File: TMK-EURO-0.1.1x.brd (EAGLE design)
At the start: 100 x 80 mm, 55 parts, among them IC1 TL082P, U1 IN, U2 IN, U3 IN, U4 IN, U5 IN, U6 IN, U7 THONKICONNOLD, X1 057-010-1

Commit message: v0.1.0.1
final V0101
INcluded board., schematic en frontpanel pcb
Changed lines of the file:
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@@
 <layer number="27" name="tValues" color="7" fill="1" visible="yes" active="yes"/>
 <layer number="28" name="bValues" color="7" fill="1" visible="yes" active="yes"/>
-<layer number="29" name="tStop" color="7" fill="3" visible="no" active="yes"/>
-<layer number="30" name="bStop" color="7" fill="6" visible="no" active="yes"/>
+<layer number="29" name="tStop" color="7" fill="3" visible="yes" active="yes"/>
+<layer number="30" name="bStop" color="7" fill="6" visible="yes" active="yes"/>
 <layer number="31" name="tCream" color="7" fill="4" visible="yes" active="yes"/>
 <layer number="32" name="bCream" color="7" fill="5" visible="yes" active="yes"/>
@@
 <text x="44.45" y="3.81" size="1.778" layer="21">1KNOB2MANY</text>
 <text x="12.7" y="1.27" size="1.27" layer="21" ratio="7">sound mangling ultra drive feedback gain  resonator</text>
+<text x="17.78" y="45.72" size="1.778" layer="25">+</text>
 </plain>
 <attributes>
@@
 </element>
 <element name="C1" library="adafruit" package="E2-5" value="10uF" x="15.24" y="44.45" smashed="yes" rot="R270">
-<attribute name="NAME" x="10.16" y="42.926" size="1.27" layer="25" ratio="10"/>
+<attribute name="NAME" x="11.43" y="41.656" size="1.27" layer="25" ratio="10"/>
 </element>
 <element name="C9" library="rcl" package="C050-035X075" value="100nF" x="91.44" y="59.69" smashed="yes" rot="R180">
@@
 <vertex x="1.27" y="77.47"/>
 <vertex x="1.27" y="0"/>
-<vertex x="99.06" y="1.27"/>
+<vertex x="99.06" y="0.635"/>
 <vertex x="99.06" y="78.74"/>
 <vertex x="24.13" y="78.74"/>
@@
 <contactref element="X1" pad="5"/>
 <contactref element="X1" pad="7"/>
-<via x="20.32" y="64.77" extent="1-16" drill="0.6" shape="square"/>
-<via x="22.86" y="66.04" extent="1-16" drill="0.6" shape="square"/>
-<via x="24.13" y="60.96" extent="1-16" drill="0.6" shape="square"/>
-<via x="26.67" y="63.5" extent="1-16" drill="0.6" shape="square"/>
+<via x="20.32" y="64.77" extent="1-16" drill="0.6" diameter="0.8128" shape="square"/>
+<via x="22.86" y="66.04" extent="1-16" drill="0.6" diameter="0.8128" shape="square"/>
+<via x="24.13" y="60.96" extent="1-16" drill="0.6" diameter="0.8128" shape="square"/>
+<via x="26.67" y="63.5" extent="1-16" drill="0.6" diameter="0.8128" shape="square"/>
 <wire x1="20.32" y1="64.77" x2="21.59" y2="63.5" width="0.6096" layer="1"/>
 <wire x1="21.59" y1="63.5" x2="24.13" y2="60.96" width="0.6096" layer="1"/>
 <wire x1="22.86" y1="66.04" x2="25.4" y2="63.5" width="0.6096" layer="1"/>
 <wire x1="25.4" y1="63.5" x2="26.67" y2="63.5" width="0.6096" layer="1"/>
-<via x="21.59" y="10.16" extent="1-16" drill="0.3048"/>
-<via x="22.86" y="10.16" extent="1-16" drill="0.3048"/>
-<via x="24.13" y="10.16" extent="1-16" drill="0.3048"/>
-<via x="21.59" y="5.08" extent="1-16" drill="0.3048"/>
-<via x="22.86" y="5.08" extent="1-16" drill="0.3048"/>
-<via x="24.13" y="5.08" extent="1-16" drill="0.3048"/>
+<via x="21.59" y="10.16" extent="1-16" drill="0.3048" diameter="0.8128"/>
+<via x="22.86" y="10.16" extent="1-16" drill="0.3048" diameter="0.8128"/>
+<via x="24.13" y="10.16" extent="1-16" drill="0.3048" diameter="0.8128"/>
+<via x="21.59" y="5.08" extent="1-16" drill="0.3048" diameter="0.8128"/>
+<via x="22.86" y="5.08" extent="1-16" drill="0.3048" diameter="0.8128"/>
+<via x="24.13" y="5.08" extent="1-16" drill="0.3048" diameter="0.8128"/>
 <wire x1="21.59" y1="5.08" x2="21.59" y2="6.35" width="0.6096" layer="1"/>
 <wire x1="21.59" y1="6.35" x2="21.59" y2="8.89" width="0.6096" layer="1"/>
@@
 <wire x1="22.86" y1="6.35" x2="22.86" y2="5.08" width="0.6096" layer="1"/>
 <wire x1="24.13" y1="10.16" x2="24.13" y2="8.89" width="0.6096" layer="1"/>
-<via x="21.59" y="8.89" extent="1-16" drill="0.3048"/>
-<via x="22.86" y="8.89" extent="1-16" drill="0.3048"/>
+<via x="21.59" y="8.89" extent="1-16" drill="0.3048" diameter="0.8128"/>
+<via x="22.86" y="8.89" extent="1-16" drill="0.3048" diameter="0.8128"/>
 <wire x1="24.13" y1="8.89" x2="24.13" y2="6.35" width="0.6096" layer="1"/>
-<via x="24.13" y="8.89" extent="1-16" drill="0.3048"/>
-<via x="21.59" y="6.35" extent="1-16" drill="0.3048"/>
-<via x="22.86" y="6.35" extent="1-16" drill="0.3048"/>
+<via x="24.13" y="8.89" extent="1-16" drill="0.3048" diameter="0.8128"/>
+<via x="21.59" y="6.35" extent="1-16" drill="0.3048" diameter="0.8128"/>
+<via x="22.86" y="6.35" extent="1-16" drill="0.3048" diameter="0.8128"/>
 <wire x1="24.13" y1="6.35" x2="24.13" y2="5.08" width="0.6096" layer="1"/>
-<via x="24.13" y="6.35" extent="1-16" drill="0.3048"/>
-<via x="21.59" y="63.5" extent="1-16" drill="0.3048"/>
+<via x="24.13" y="6.35" extent="1-16" drill="0.3048" diameter="0.8128"/>
+<via x="21.59" y="63.5" extent="1-16" drill="0.5" diameter="0.8128"/>
 </signal>
 <signal name="N$2" class="2">

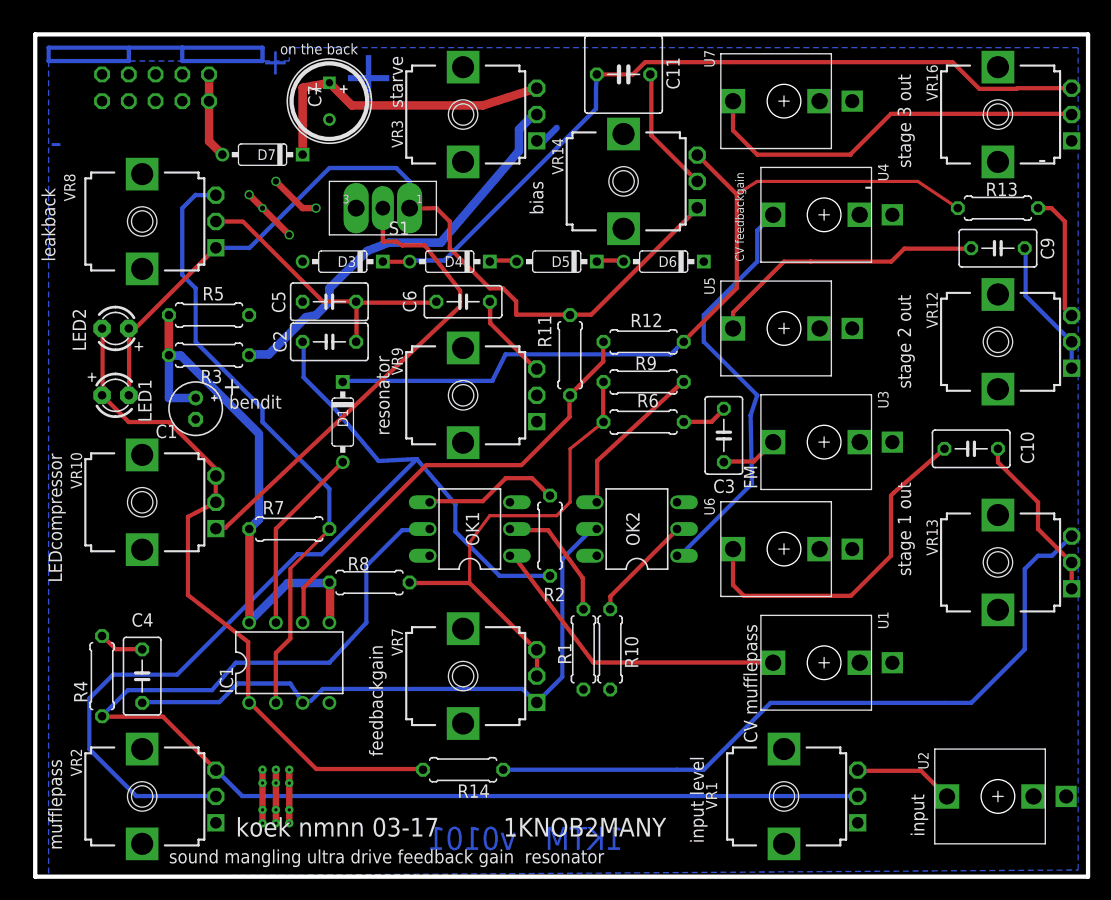
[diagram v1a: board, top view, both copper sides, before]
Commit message: Cleanup for errors
Removed all the CV-inputs. Fixed the power. Check this on breadboard
first!
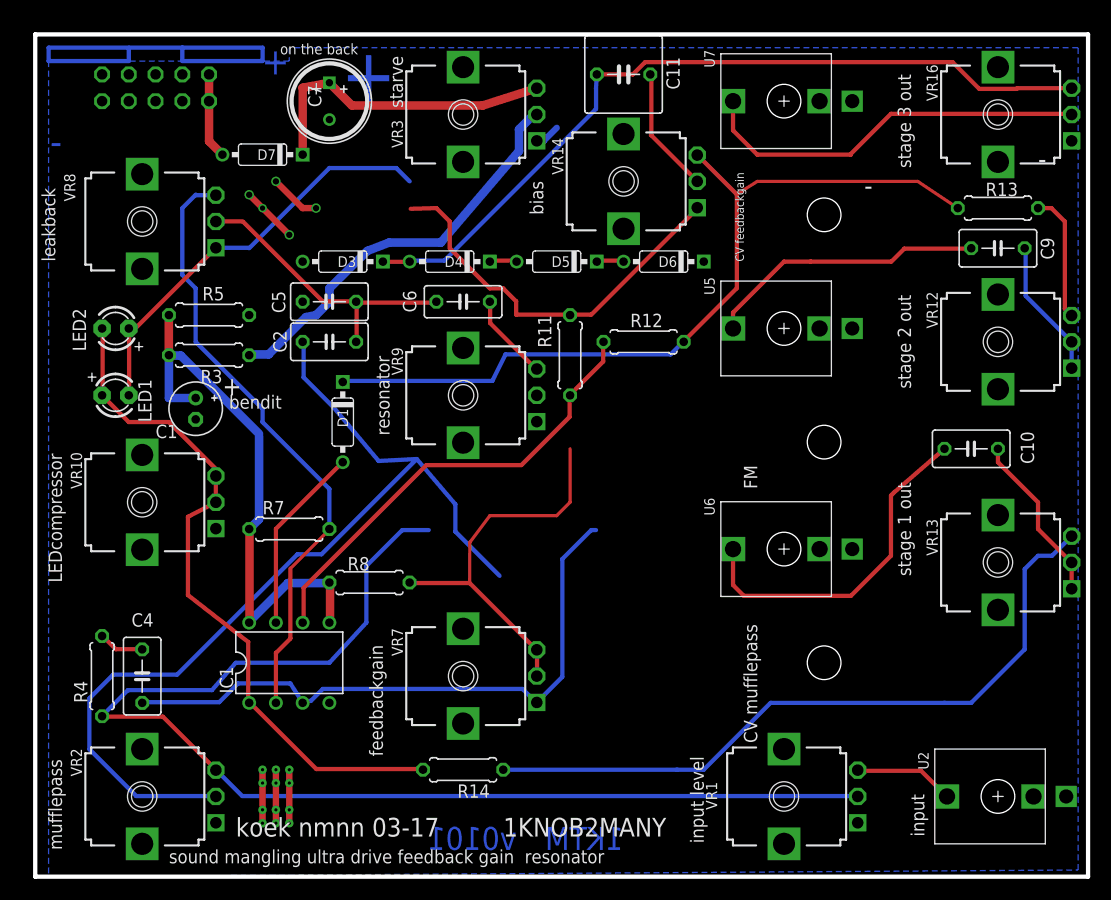
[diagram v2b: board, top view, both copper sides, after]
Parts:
- removed C3: 100nF, rcl:C050-035X075
- removed OK1, OK2: 4N35, optocoupler:DIL06
- removed R1, R10: 5K6, adafruit:0207/7
- removed R2, R9: 3K3, adafruit:0207/7
- removed R6: 10K, adafruit:0207/7
- removed S1: (no value), momentswitchREDlveewrergalmoer mini switch:SPDT
- removed U1, U3, U4: IN, MusicThingModular:THONKICONN
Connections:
- removed net BYPASS: S1.2, VR10.1
- removed net N$27: OK2.4, R9.2
- removed net N$28: OK2.2, R10.1
- removed net N$30: OK2.1, U4.P$3_TIP
- removed net N$31: OK1.4, R2.1
- removed net N$32: OK1.2, R1.1
- removed net N$33: OK1.1, U1.P$3_TIP
- removed net N$34: S1.3
- removed net N$36: C3.1, R6.2
- removed net N$37: C3.2, U3.P$3_TIP
- removed net N$4: C4.2, IC1.3, OK2.5, VR7.1
- new net N$26: C4.2, IC1.3, VR7.1
- net GND: no longer R1.2, R10.2, U1.P$1_SLEEVE, U3.P$1_SLEEVE, U4.P$1_SLEEVE
- net N$2: no longer OK1.5
- net N$5: no longer R6.1, R9.1
- net N$7: now also VR10.1; no longer S1.1
- net N$9: no longer R2.2
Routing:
- net N$4: track 59.5 -> 0.00 mm
- net N$26: track 0.00 -> 59.4 mm
- net BYPASS: track 45.8 -> 0.00 mm
- net N$30: track 40.4 -> 0.00 mm
- net N$33: track 30.1 -> 0.00 mm
- net N$27: track 15.1 -> 0.00 mm
- net N$31: track 13.1 -> 0.00 mm
- net N$32: track 12.3 -> 0.00 mm
- net N$28: track 10.2 -> 0.00 mm
- net N$5: track 45.5 -> 37.5 mm
- net N$37: track 5.47 -> 0.00 mm
- net N$9: track 95.9 -> 91.1 mm
- net N$36: track 4.38 -> 0.00 mm
- net N$7: track 80.6 -> 77.8 mm

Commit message: Fixed power
No Vr on power pin 8, but 12V from the main power supply
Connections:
- net +12V: now also IC1.8
- net VR: no longer IC1.8
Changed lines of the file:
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@@
 <contactref element="R5" pad="1"/>
 <contactref element="C1" pad="+"/>
-<contactref element="IC1" pad="8"/>
 <wire x1="12.6873" y1="53.2638" x2="12.6873" y2="49.6062" width="0.8128" layer="1"/>
 <wire x1="12.6873" y1="49.6062" x2="12.7" y2="49.53" width="0.4064" layer="1"/>
@@
 <wire x1="28.0035" y1="27.8892" x2="27.94" y2="27.94" width="0.4064" layer="1"/>
 <wire x1="20.3454" y1="32.9184" x2="20.3454" y2="24.2316" width="0.8128" layer="1"/>
-<wire x1="20.3454" y1="24.2316" x2="20.32" y2="24.13" width="0.4064" layer="1"/>
 <wire x1="20.3454" y1="32.9184" x2="20.32" y2="33.02" width="0.4064" layer="1"/>
 <wire x1="21.2598" y1="33.9471" x2="21.2598" y2="41.8338" width="0.8128" layer="16"/>
@@
 <wire x1="20.3454" y1="24.2316" x2="24.003" y2="27.8892" width="0.8128" layer="16"/>
 <wire x1="27.8892" y1="27.8892" x2="27.94" y2="27.94" width="0.4064" layer="16"/>
-<wire x1="20.3454" y1="24.2316" x2="20.32" y2="24.13" width="0.4064" layer="16"/>
 <wire x1="13.8303" y1="49.4919" x2="12.8016" y2="49.4919" width="0.8128" layer="16"/>
 <wire x1="21.2598" y1="42.0624" x2="13.8303" y2="49.4919" width="0.8128" layer="16"/>
@@
 <wire x1="12.7" y1="45.466" x2="12.7" y2="49.53" width="0.8128" layer="16"/>
 <wire x1="21.2598" y1="41.8338" x2="21.2598" y2="42.0624" width="0" layer="19" extent="16-16"/>
+<wire x1="20.3454" y1="24.2316" x2="20.3454" y2="24.2316" width="0" layer="19" extent="1-16"/>
 </signal>
 <signal name="N$7" class="1">
@@
 <wire x1="25.4" y1="74.93" x2="27.94" y2="75.41" width="0.8128" layer="1"/>
 <wire x1="25.4" y1="68.58" x2="25.4" y2="74.93" width="0.8128" layer="1"/>
+<contactref element="IC1" pad="8"/>
 <wire x1="27.94" y1="75.41" x2="28.1178" y2="75.2094" width="0" layer="19" extent="1-1"/>
+<wire x1="20.32" y1="24.13" x2="25.4" y2="68.58" width="0" layer="19" extent="1-1"/>
 </signal>
 <signal name="N$20" class="2">

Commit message: Nets netjes
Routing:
- net N$4: track 12.3 -> 0.00 mm
- net N$13: track 78.1 -> 73.4 mm
- net OUTPUT2: track 14.9 -> 11.5 mm
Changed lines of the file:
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@@
 <contactref element="R12" pad="2"/>
 <contactref element="D1" pad="C"/>
-<contactref element="R13" pad="2"/>
 <wire x1="62.9793" y1="68.4657" x2="66.6369" y2="64.8081" width="0.4064" layer="1"/>
-<wire x1="87.63" y1="63.5" x2="87.5538" y2="63.5381" width="0.4064" layer="1"/>
 <wire x1="62.9793" y1="68.4657" x2="62.88" y2="68.54" width="0.4064" layer="1"/>
 <wire x1="43.4213" y1="47.0916" x2="29.2608" y2="47.0916" width="0.4064" layer="16"/>
@@
 <wire x1="66.6369" y1="64.8081" x2="68.58" y2="66.04" width="0.3048" layer="1"/>
 <wire x1="68.58" y1="66.04" x2="83.82" y2="66.04" width="0.3048" layer="1"/>
-<wire x1="83.82" y1="66.04" x2="87.63" y2="63.5" width="0.3048" layer="1"/>
+<contactref element="R13" pad="2"/>
+<wire x1="83.82" y1="66.04" x2="87.63" y2="63.5" width="0" layer="19" extent="1-1"/>
 </signal>
 <signal name="N$14">
@@
 <wire x1="98.4123" y1="50.7365" x2="98.44" y2="50.8" width="0.4064" layer="16"/>
 <wire x1="98.44" y1="50.8" x2="98.5266" y2="50.8508" width="0.4064" layer="1"/>
-<contactref element="VR12" pad="1"/>
 <wire x1="94.0689" y1="59.6519" x2="94.0689" y2="55.1711" width="0.4064" layer="16"/>
 <wire x1="94.0689" y1="55.1711" x2="98.44" y2="50.8" width="0.4064" layer="16"/>
 <wire x1="98.44" y1="50.8" x2="97.8408" y2="50.8" width="0.1524" layer="16"/>
-<wire x1="98.44" y1="48.3" x2="97.8408" y2="47.7008" width="0.4064" layer="16"/>
-<wire x1="98.44" y1="50.8" x2="98.44" y2="48.3" width="0.4064" layer="16"/>
+<contactref element="VR12" pad="1"/>
+<wire x1="98.44" y1="48.3" x2="98.4123" y2="50.7365" width="0" layer="19" extent="16-16"/>
 </signal>
 <signal name="N$35" class="2">
@@
 <wire x1="95.25" y1="30.48" x2="96.575" y2="30.48" width="0.4064" layer="16"/>
 <wire x1="96.575" y1="30.48" x2="98.44" y2="32.345" width="0.4064" layer="16"/>
-</signal>
-<signal name="N$17">
-<contactref element="R13" pad="1"/>
-<contactref element="VR12" pad="3"/>
-<wire x1="95.25" y1="63.5" x2="96.52" y2="63.5" width="0.4064" layer="1"/>
-<wire x1="96.52" y1="63.5" x2="97.79" y2="62.23" width="0.4064" layer="1"/>
-<wire x1="97.79" y1="53.95" x2="98.44" y2="53.3" width="0.4064" layer="1"/>
-<wire x1="97.79" y1="62.23" x2="97.79" y2="53.95" width="0.4064" layer="1"/>
 </signal>
 <signal name="N$26" class="2">
@@
 <wire x1="47.5488" y1="16.5735" x2="47.64" y2="16.55" width="0.4064" layer="16"/>
 </signal>
+<signal name="N$4">
+<contactref element="R13" pad="1"/>
+<contactref element="VR12" pad="3"/>
+<wire x1="98.44" y1="53.3" x2="95.25" y2="63.5" width="0" layer="19" extent="1-1"/>
+</signal>
 </signals>
